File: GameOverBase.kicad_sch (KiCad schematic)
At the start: 51 parts, among them J1 USB_C_Receptacle_USB2.0, J2 Serial Port, J3 add-on conn, Q1 PMN48XP, SW1 SW_DIP_x08, SW2 Reset, SW3 Reset, U1 ESP32-WROOM-E, U2 4021, U3 MCP73831-2ACI-OT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

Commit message: Adds footprint for PTC fuses
We're using the Belfuse 0ZCJ fuses, but we need to make sure we buy one
with the same footprint (or change it later).
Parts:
- BT1: footprint (none) -> Connector_JST:JST_PH_S2B-PH-SM4-TB_1x02-1MP_P2.00mm_Horizontal
- C1, C10, C11, C12, C13, C14, C2, C3, C4, C5, C6, C7, C8, C9: footprint (none) -> Capacitor_SMD:C_0805_2012Metric_Pad1.18x1.45mm_HandSolder
- D1: footprint (none) -> Diode_SMD:D_SOD-123
- D2: footprint (none) -> LED_SMD:LED_0805_2012Metric_Pad1.15x1.40mm_HandSolder
- R1, R10, R11, R12, R13, R14, R15, R16, R17, R18, R19, R2, R20, R3, R4, R5, R6, R7, R8, R9: footprint (none) -> Resistor_SMD:R_0805_2012Metric_Pad1.20x1.40mm_HandSolder
- U2: footprint (none) -> Package_SO:TSSOP-16-1EP_4.4x5mm_P0.65mm

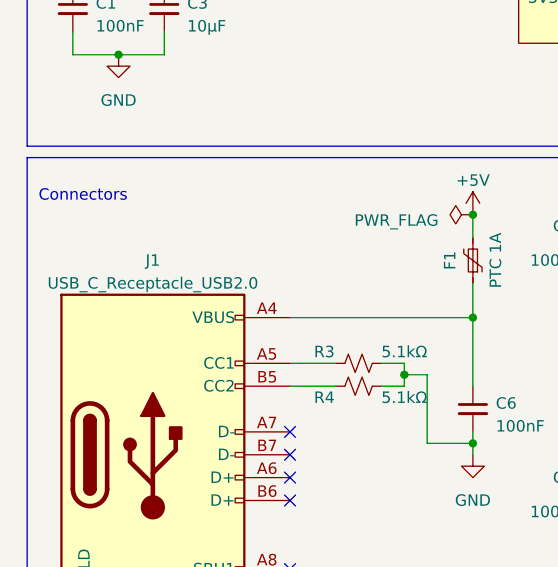
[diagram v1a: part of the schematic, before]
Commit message: Adds footprint for USB-C (power only) connector
We're using the DEALON USB-US31-106.
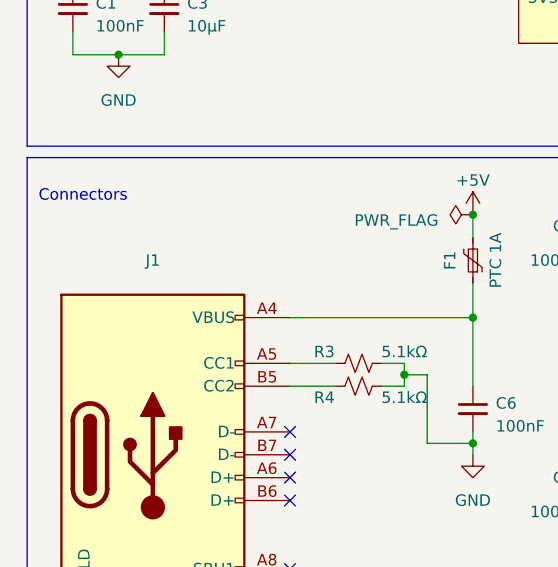
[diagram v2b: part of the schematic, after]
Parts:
- F1, F2: footprint (none) -> GameOver:Belfuse_0ZCJ
- J1: value USB_C_Receptacle_USB2.0 -> (none)
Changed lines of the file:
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@@
       (effects (font (size 1.27 1.27)))
     )
-    (property "Footprint" "" (id 2) (at 269.24 80.01 0)
+    (property "Footprint" "GameOver:Belfuse_0ZCJ" (id 2) (at 269.24 80.01 0)
       (effects (font (size 1.27 1.27)) (justify left) hide)
     )
@@
       (effects (font (size 1.27 1.27)))
     )
-    (property "Value" "USB_C_Receptacle_USB2.0" (id 1) (at 27.94 135.89 0)
+    (property "Value" "" (id 1) (at 27.94 135.89 0)
       (effects (font (size 1.27 1.27)))
     )
@@
       (effects (font (size 1.27 1.27)))
     )
-    (property "Footprint" "" (id 2) (at 62.23 128.27 0)
+    (property "Footprint" "GameOver:Belfuse_0ZCJ" (id 2) (at 62.23 128.27 0)
       (effects (font (size 1.27 1.27)) (justify left) hide)
     )
@@
     )
     (path "/60060b39-57f0-4f2c-a062-c391396cf2bf"
-      (reference "J1") (unit 1) (value "USB_C_Receptacle_USB2.0") (footprint "")
+      (reference "J1") (unit 1) (value "USB_C_Receptacle_USB2.0") (footprint "GameOver:DEALON_USB-US31-106")
     )
     (path "/a4a4a9b2-b00e-4de8-947c-82cb95b02a26"

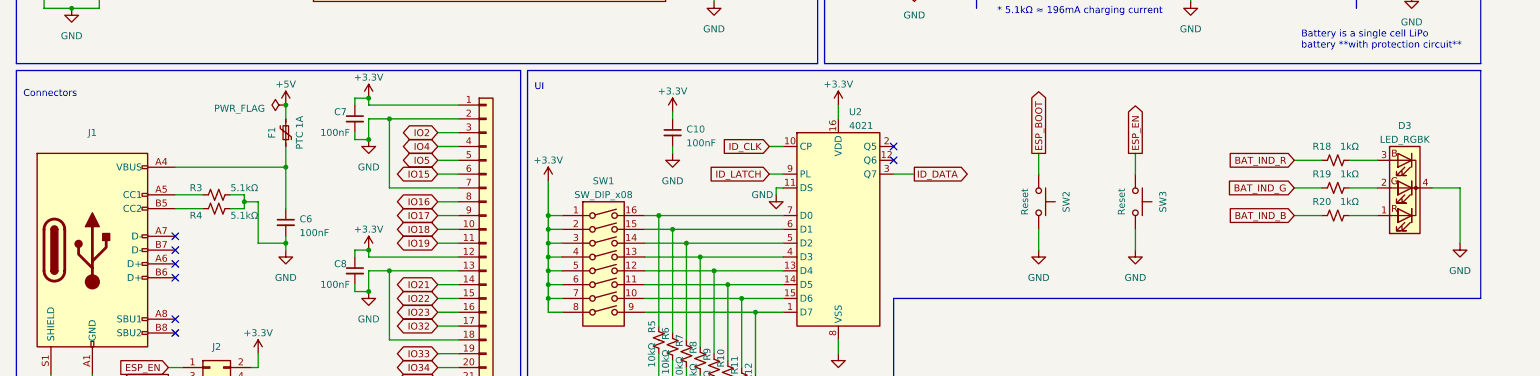
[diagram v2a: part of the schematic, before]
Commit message: Changes RGB led for battery indication to common anode
This is the kind of LED we bought
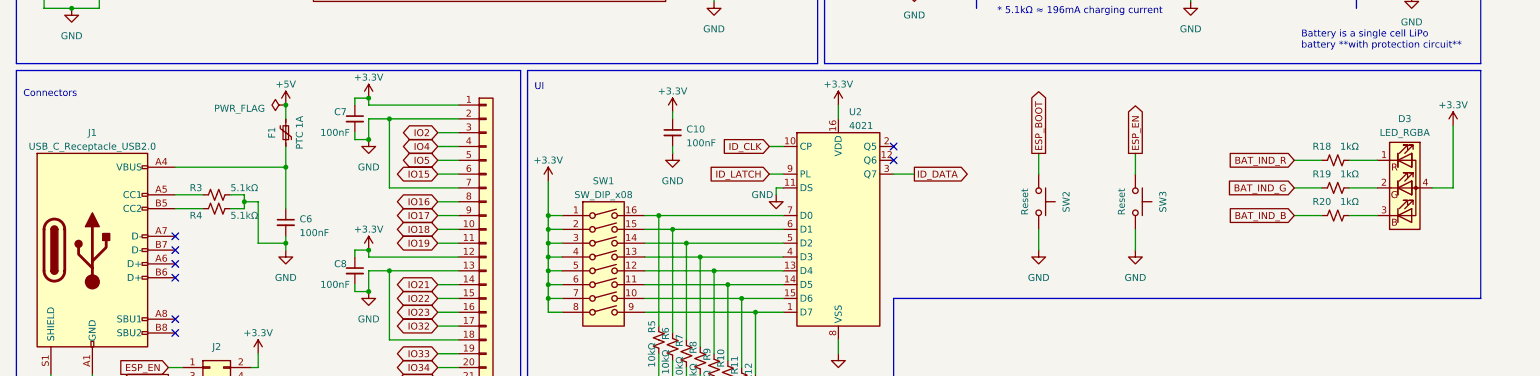
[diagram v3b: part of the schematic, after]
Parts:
- removed D3: LED_RGBK, symbol Device:LED_RGBK
- added D3: LED_RGBA, symbol Device:LED_RGBA
- J1: value (none) -> USB_C_Receptacle_USB2.0; footprint (none) -> GameOver:DEALON_USB-US31-106
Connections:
- net +3V3: now also D3.4 (A)
- net at R20.2: now also D3.3 (BK)
- net at R18.2: now also D3.1 (RK)
- net at R19.2: now also D3.2 (GK)
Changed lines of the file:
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@@
     (stroke (width 0) (type default))
   )
+  (wire (pts (xy 278.13 143.51) (xy 278.13 132.08))
+    (stroke (width 0) (type default))
+  )
   (wire (pts (xy 62.23 95.25) (xy 66.04 95.25))
     (stroke (width 0) (type default))
@@
     (stroke (width 0) (type default))
   )
-  (wire (pts (xy 274.32 143.51) (xy 279.4 143.51))
-    (stroke (width 0) (type default))
-  )
   (wire (pts (xy 134.62 180.34) (xy 137.16 180.34))
     (stroke (width 0) (type default))
@@
     (stroke (width 0) (type default))
   )
+  (wire (pts (xy 274.32 143.51) (xy 278.13 143.51))
+    (stroke (width 0) (type default))
+  )
   (wire (pts (xy 248.92 143.51) (xy 254 143.51))
     (stroke (width 0) (type default))
@@
     (stroke (width 0) (type default))
   )
-  (wire (pts (xy 279.4 143.51) (xy 279.4 153.67))
-    (stroke (width 0) (type default))
-  )
   (wire (pts (xy 144.78 161.29) (xy 154.94 161.29))
     (stroke (width 0) (type default))
@@
       (effects (font (size 1.27 1.27)))
     )
-    (property "Value" "" (id 1) (at 27.94 135.89 0)
+    (property "Value" "USB_C_Receptacle_USB2.0" (id 1) (at 27.94 135.89 0)
       (effects (font (size 1.27 1.27)))
     )
-    (property "Footprint" "" (id 2) (at 31.75 154.94 0)
+    (property "Footprint" "GameOver:DEALON_USB-US31-106" (id 2) (at 31.75 154.94 0)
       (effects (font (size 1.27 1.27)) hide)
     )
@@
     (pin "1")
   )
-  (symbol (lib_id "power:GND") (at 279.4 153.67 0) (unit 1)
+  (symbol (lib_id "power:PWR_FLAG") (at 184.15 59.69 270) (unit 1)
     (in_bom yes) (on_board yes) (fields_autoplaced)
-    (property "Reference" "#PWR048" (id 0) (at 279.4 160.02 0)
+    (property "Reference" "#FLG02" (id 0) (at 186.055 59.69 0)
       (effects (font (size 1.27 1.27)) hide)
     )
-    (property "Value" "GND" (id 1) (at 279.4 158.75 0)
-      (effects (font (size 1.27 1.27)))
+    (property "Value" "PWR_FLAG" (id 1) (at 187.96 60.325 90)
+      (effects (font (size 1.27 1.27)) (justify left))
     )
-    (property "Footprint" "" (id 2) (at 279.4 153.67 0)
+    (property "Footprint" "" (id 2) (at 184.15 59.69 0)
       (effects (font (size 1.27 1.27)) hide)
     )
-    (property "Datasheet" "" (id 3) (at 279.4 153.67 0)
+    (property "Datasheet" "~" (id 3) (at 184.15 59.69 0)
       (effects (font (size 1.27 1.27)) hide)
     )
     (pin "1")
   )
-  (symbol (lib_id "power:PWR_FLAG") (at 184.15 59.69 270) (unit 1)
+  (symbol (lib_id "power:+3.3V") (at 278.13 132.08 0) (unit 1)
     (in_bom yes) (on_board yes) (fields_autoplaced)
-    (property "Reference" "#FLG02" (id 0) (at 186.055 59.69 0)
+    (property "Reference" "#PWR048" (id 0) (at 278.13 135.89 0)
       (effects (font (size 1.27 1.27)) hide)
     )
-    (property "Value" "PWR_FLAG" (id 1) (at 187.96 60.325 90)
-      (effects (font (size 1.27 1.27)) (justify left))
+    (property "Value" "+3.3V" (id 1) (at 278.13 128.27 0)
+      (effects (font (size 1.27 1.27)))
     )
-    (property "Footprint" "" (id 2) (at 184.15 59.69 0)
+    (property "Footprint" "" (id 2) (at 278.13 132.08 0)
       (effects (font (size 1.27 1.27)) hide)
     )
-    (property "Datasheet" "~" (id 3) (at 184.15 59.69 0)
+    (property "Datasheet" "" (id 3) (at 278.13 132.08 0)
       (effects (font (size 1.27 1.27)) hide)
     )
@@
     (pin "1")
   )
+  (symbol (lib_id "Device:LED_RGBA") (at 269.24 143.51 0) (unit 1)
+    (in_bom yes) (on_board yes) (fields_autoplaced)
+    (property "Reference" "D3" (id 0) (at 269.24 130.81 0)
+      (effects (font (size 1.27 1.27)))
+    )
+    (property "Value" "LED_RGBA" (id 1) (at 269.24 133.35 0)
+      (effects (font (size 1.27 1.27)))
+    )
+    (property "Footprint" "" (id 2) (at 269.24 144.78 0)
+      (effects (font (size 1.27 1.27)) hide)
+    )
+    (property "Datasheet" "~" (id 3) (at 269.24 144.78 0)
+      (effects (font (size 1.27 1.27)) hide)
+    )
+    (pin "1")
+    (pin "2")
+    (pin "3")
+    (pin "4")
+  )
   (symbol (lib_id "power:GND") (at 229.87 109.22 0) (unit 1)
     (in_bom yes) (on_board yes) (fields_autoplaced)
@@
     (pin "2")
   )
-  (symbol (lib_id "Device:LED_RGBK") (at 269.24 143.51 180) (unit 1)
-    (in_bom yes) (on_board yes) (fields_autoplaced)
-    (property "Reference" "D3" (id 0) (at 269.24 132.08 0)
-      (effects (font (size 1.27 1.27)))
-    )
-    (property "Value" "LED_RGBK" (id 1) (at 269.24 134.62 0)
-      (effects (font (size 1.27 1.27)))
-    )
-    (property "Footprint" "" (id 2) (at 269.24 142.24 0)
-      (effects (font (size 1.27 1.27)) hide)
-    )
-    (property "Datasheet" "~" (id 3) (at 269.24 142.24 0)
-      (effects (font (size 1.27 1.27)) hide)
-    )
-    (pin "1")
-    (pin "2")
-    (pin "3")
-    (pin "4")
-  )
   (symbol (lib_id "Device:R_Small_US") (at 184.15 52.07 0) (unit 1)
     (in_bom yes) (on_board yes) (fields_autoplaced)
@@
       (reference "#PWR047") (unit 1) (value "GND") (footprint "")
     )
-    (path "/86c8178b-09c7-44f9-88a1-f9fe1a5bdd6e"
-      (reference "#PWR048") (unit 1) (value "GND") (footprint "")
+    (path "/917ef960-c29b-45aa-8bf0-ec19fc5f2def"
+      (reference "#PWR048") (unit 1) (value "+3.3V") (footprint "")
     )
     (path "/bddc0e5f-3e5c-408f-b78e-2737418bc360"
@@
       (reference "D2") (unit 1) (value "green") (footprint "LED_SMD:LED_0805_2012Metric_Pad1.15x1.40mm_HandSolder")
     )
-    (path "/fd178625-dfd8-4276-963d-bb14af20f0ab"
-      (reference "D3") (unit 1) (value "LED_RGBK") (footprint "")
+    (path "/ce826760-c436-4f38-8b7b-056ff6dcb9d9"
+      (reference "D3") (unit 1) (value "LED_RGBA") (footprint "")
     )
     (path "/cc111127-f001-4494-a46a-df9cfd9d4666"

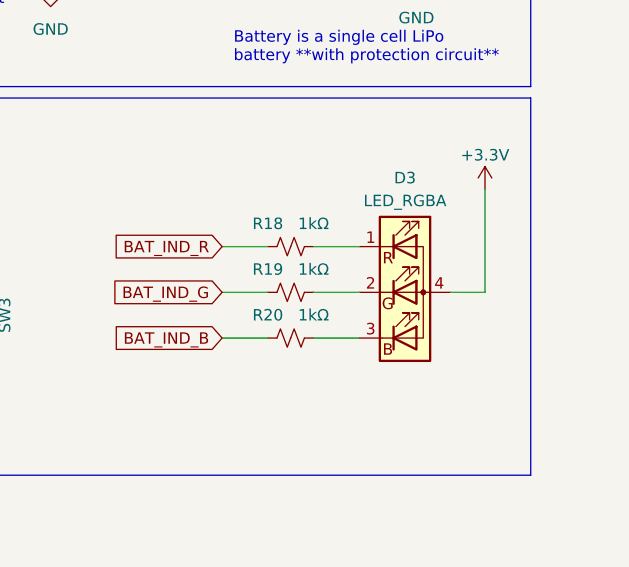
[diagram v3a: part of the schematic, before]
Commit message: Switches pins on RGB led based on the actual part we bought
We'll be using the Hongzhi Forest HS-1204-RGB
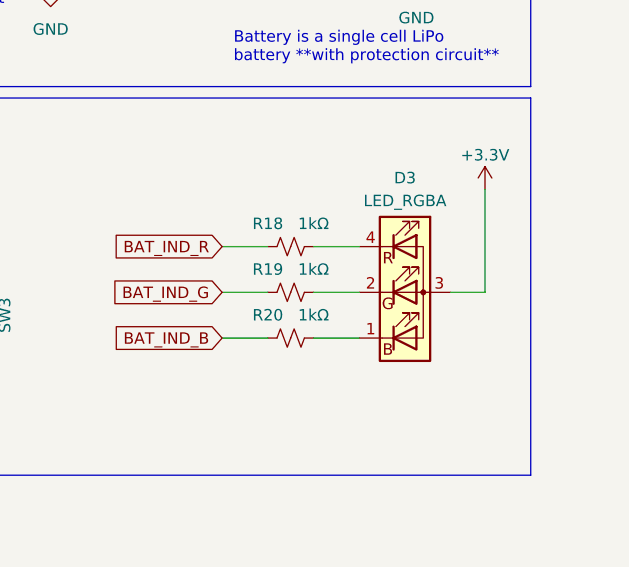
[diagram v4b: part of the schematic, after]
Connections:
- net +3V3: now also D3.3 (A); no longer D3.4 (A)
- net at R20.2: now also D3.1 (BK); no longer D3.3 (BK)
- net at R18.2: now also D3.4 (RK); no longer D3.1 (RK)
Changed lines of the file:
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@@
       (effects (font (size 1.27 1.27)) hide)
     )
+    (pin "4")
+    (pin "2")
     (pin "1")
-    (pin "2")
     (pin "3")
-    (pin "4")
   )
   (symbol (lib_id "power:GND") (at 229.87 109.22 0) (unit 1)

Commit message: Adds footprint for the Hongzhi Forest HS-1204-RGB LED
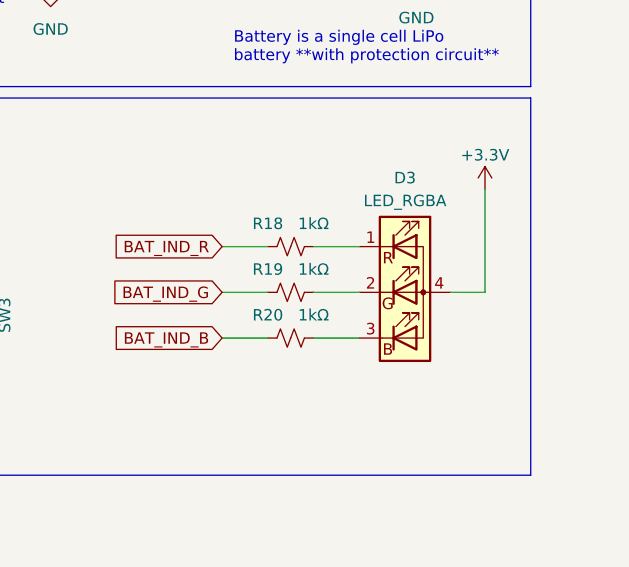
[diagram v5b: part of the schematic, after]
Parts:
- D3: footprint (none) -> GameOver:Hongzhi_Forest_HS-1204-RGB
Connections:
- net +3V3: now also D3.4 (A); no longer D3.3 (A)
- net at R20.2: now also D3.3 (BK); no longer D3.1 (BK)
- net at R18.2: now also D3.1 (RK); no longer D3.4 (RK)
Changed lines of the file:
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@@
       (effects (font (size 1.27 1.27)))
     )
-    (property "Footprint" "" (id 2) (at 269.24 144.78 0)
+    (property "Footprint" "GameOver:Hongzhi_Forest_HS-1204-RGB" (id 2) (at 269.24 144.78 0)
       (effects (font (size 1.27 1.27)) hide)
     )
@@
       (effects (font (size 1.27 1.27)) hide)
     )
+    (pin "1")
+    (pin "2")
+    (pin "3")
     (pin "4")
-    (pin "2")
-    (pin "1")
-    (pin "3")
   )
   (symbol (lib_id "power:GND") (at 229.87 109.22 0) (unit 1)
@@
     )
     (path "/ce826760-c436-4f38-8b7b-056ff6dcb9d9"
-      (reference "D3") (unit 1) (value "LED_RGBA") (footprint "")
+      (reference "D3") (unit 1) (value "LED_RGBA") (footprint "GameOver:Hongzhi_Forest_HS-1204-RGB")
     )
     (path "/cc111127-f001-4494-a46a-df9cfd9d4666"

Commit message: Adds footprint for TXGA FFC05036-24SBD113W5M
This is the FFC connector we'll use to connect the base to other boards
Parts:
- J3: footprint (none) -> GameOver:TXGA_FFC05036-24SBD113W5M_1x24_P0.50mm_Horizontal
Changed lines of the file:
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@@
       (effects (font (size 1.27 1.27)) (justify left))
     )
-    (property "Footprint" "" (id 2) (at 100.33 156.21 0)
+    (property "Footprint" "GameOver:TXGA_FFC05036-24SBD113W5M_1x24_P0.50mm_Horizontal" (id 2) (at 100.33 156.21 0)
       (effects (font (size 1.27 1.27)) hide)
     )
@@
     )
     (path "/b96389fd-4b84-4e6a-b451-5d6147af997a"
-      (reference "J3") (unit 1) (value "add-on conn") (footprint "")
+      (reference "J3") (unit 1) (value "add-on conn") (footprint "GameOver:TXGA_FFC05036-24SBD113W5M_1x24_P0.50mm_Horizontal")
     )
     (path "/7812657a-77a5-4738-bb49-ebee91b9814f"

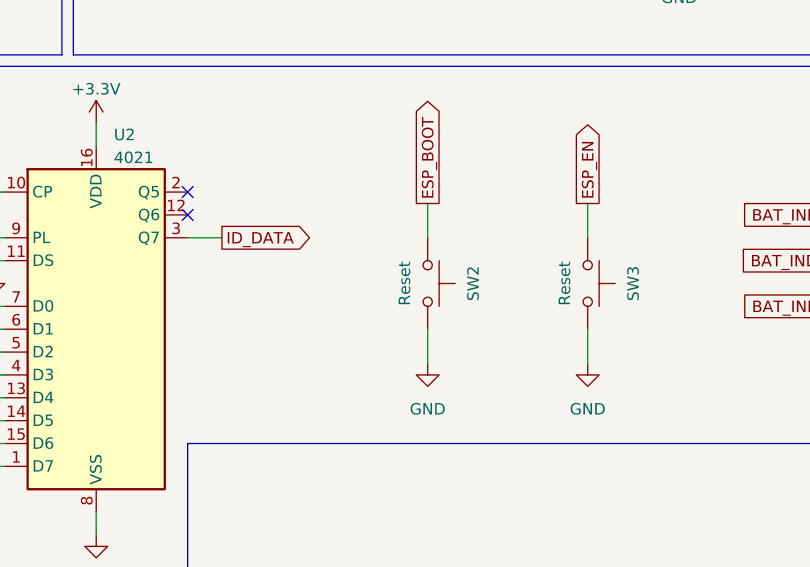
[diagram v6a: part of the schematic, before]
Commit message: Fixes label on boot button
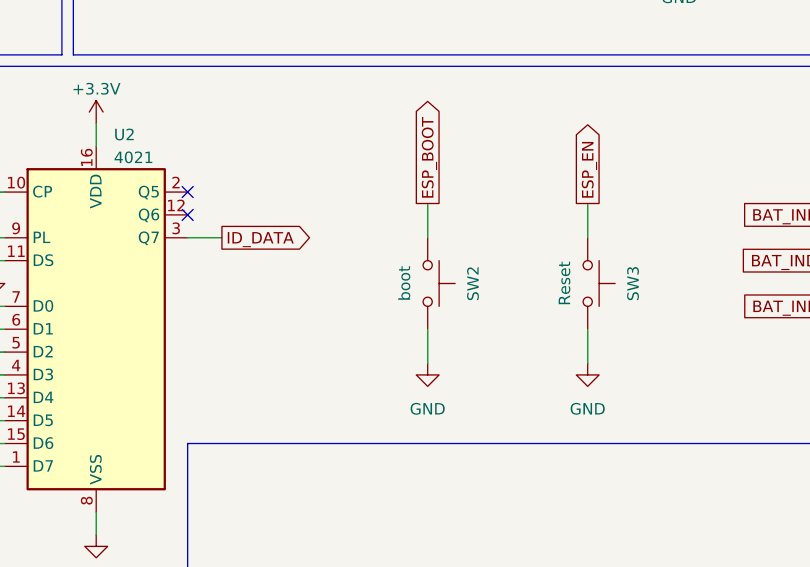
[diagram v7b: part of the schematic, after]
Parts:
- SW2: value Reset -> boot
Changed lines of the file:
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@@
       (effects (font (size 1.27 1.27)))
     )
-    (property "Value" "Reset" (id 1) (at 199.39 146.05 0)
+    (property "Value" "boot" (id 1) (at 199.39 146.05 0)
       (effects (font (size 1.27 1.27)))
     )
@@
     )
     (path "/fbfbda5b-3f1a-4559-9c00-adeb4e1f53ab"
-      (reference "SW2") (unit 1) (value "Reset") (footprint "")
+      (reference "SW2") (unit 1) (value "boot") (footprint "")
     )
     (path "/127be547-9fbb-4f55-a1d1-e12de114ea72"
